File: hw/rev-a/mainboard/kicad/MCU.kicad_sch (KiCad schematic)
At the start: 34 parts, among them J23 MENU_HDR, SW4 RUN, SW5 MENU_BTN, U21 RP2040, Y1 12 MHz

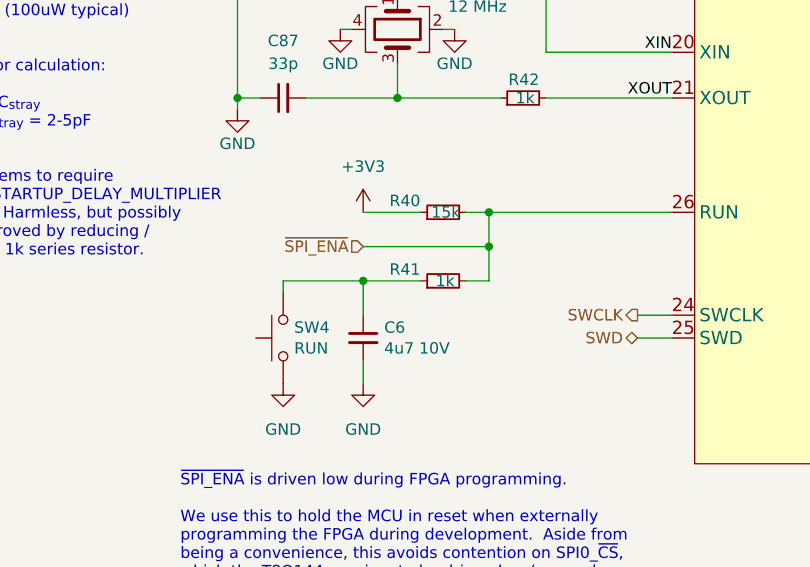
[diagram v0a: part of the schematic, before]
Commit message: hw: use stronger pullup on RUN / SPI_EN, remove debouncing cap
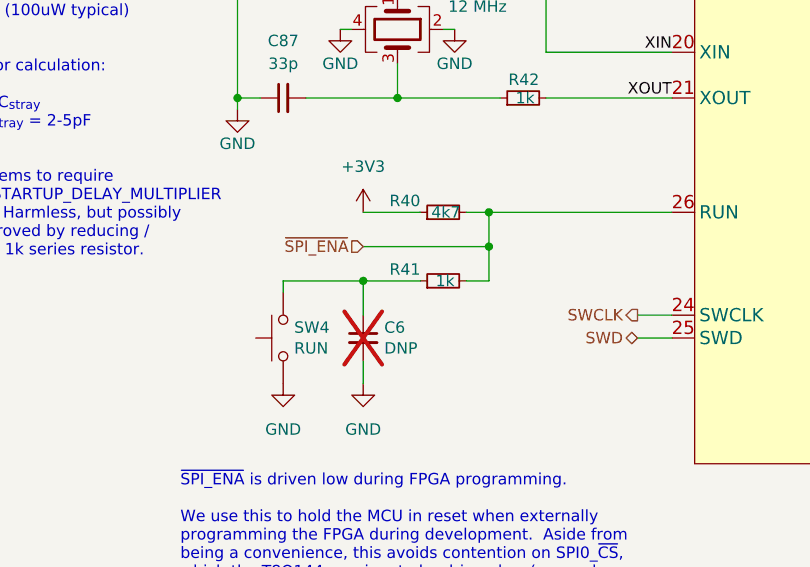
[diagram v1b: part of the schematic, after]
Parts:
- C6: value 4u7 10V -> DNP; LCSC C23733 -> (none); now not fitted
- R40: value 15k -> 4k7; LCSC C25756 -> C25900
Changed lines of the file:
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@@
 		(in_bom yes)
 		(on_board yes)
-		(dnp no)
+		(dnp yes)
 		(property "Reference" "C6"
 			(at 69.6468 120.7516 0)
@@
 			)
 		)
-		(property "Value" "4u7 10V"
+		(property "Value" "DNP"
 			(at 69.6468 123.063 0)
 			(effects
@@
 			)
 		)
-		(property "Datasheet" "https://product.samsungsem.com/mlcc/CL05A475MP5NRN.do"
+		(property "Datasheet" ""
 			(at 67.31 121.92 0)
 			(effects
@@
 			)
 		)
-		(property "LCSC" "C23733"
+		(property "LCSC" ""
 			(at 67.31 121.92 0)
 			(effects
@@
 			)
 		)
-		(property "Value" "15k"
+		(property "Value" "4k7"
 			(at 78.105 107.95 90)
 			(effects
@@
 			)
 		)
-		(property "Datasheet" "https://www.lcsc.com/datasheet/lcsc_datasheet_2206010100_UNI-ROYAL-Uniroyal-Elec-0402WGF1502TCE_C25756.pdf"
+		(property "Datasheet" "https://www.lcsc.com/datasheet/lcsc_datasheet_2206010045_UNI-ROYAL-Uniroyal-Elec-0402WGF4701TCE_C25900.pdf"
 			(at 76.2 107.95 0)
 			(effects
@@
 			)
 		)
-		(property "LCSC" "C25756"
+		(property "LCSC" "C25900"
 			(at 76.2 107.95 0)
 			(effects

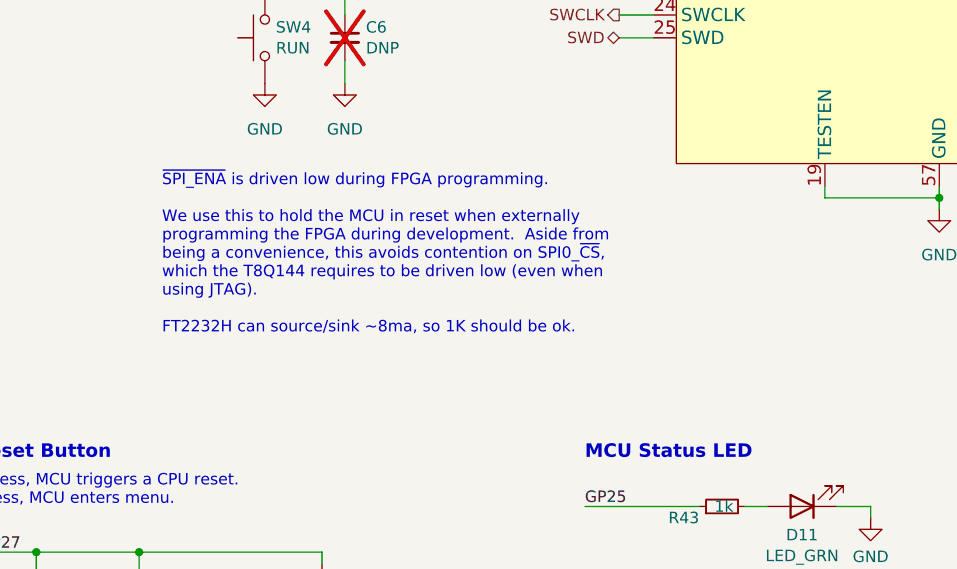
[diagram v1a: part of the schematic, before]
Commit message: hw: document JTAG / RP2040 interaction
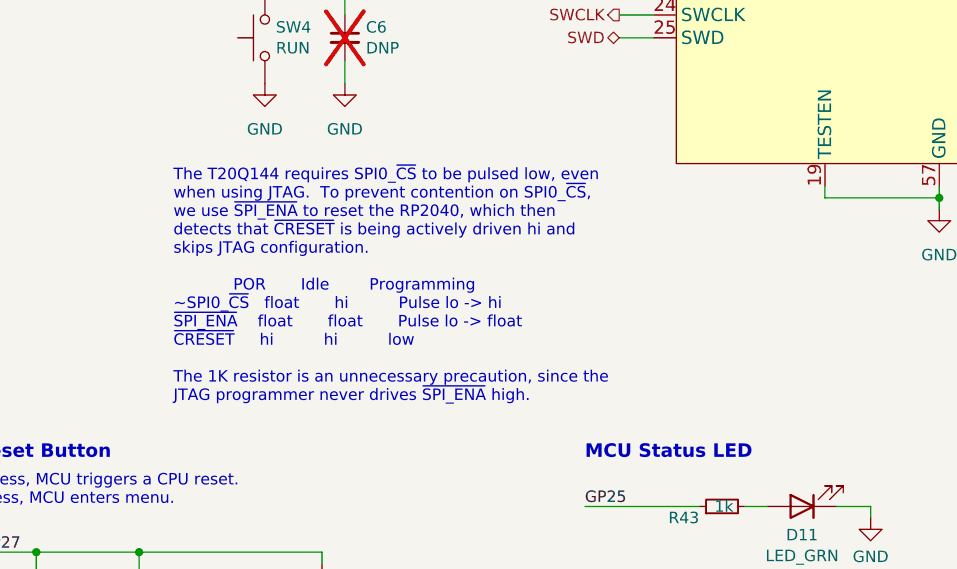
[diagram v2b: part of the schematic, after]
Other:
- note added: "The T20Q144 requires SPI0_~{CS} to be pulsed low, even when using JTAG. To prevent contention on SPI0_~{CS}, we use ~{SPI_ENA} to reset the RP2040, which then detects that ~{CRESET} is being actively driven hi and skips JTAG configuration. POR Idle Programming ~SPI0_~{CS} float hi Pulse lo -> hi ~{SPI_ENA} float float Pulse lo -> float ~{CRESET} hi hi low The 1K resistor is an unnecessary precaut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"
- note removed: "~{SPI_ENA} is driven low during FPGA programming. We use this to hold the MCU in reset when externally programming the FPGA during development. Aside from being a convenience, this avoids contention on SPI0_~{CS}, which the T8Q144 requires to be driven low (even when using JTAG). FT2232H can source/sink ~8ma, so 1K should be ok."
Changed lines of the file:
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@@
 		)
 	)
-	(text "~{SPI_ENA} is driven low during FPGA programming.\n\nWe use this to hold the MCU in reset when externally\nprogramming the FPGA during development.  Aside from\nbeing a convenience, this avoids contention on SPI0_~{CS},\nwhich the T8Q144 requires to be driven low (even when\nusing JTAG).\n\nFT2232H can source/sink ~8ma, so 1K should be ok.\n"
+	(text "The T20Q144 requires SPI0_~{CS} to be pulsed low, even\nwhen using JTAG.  To prevent contention on SPI0_~{CS},\nwe use ~{SPI_ENA} to reset the RP2040, which then\ndetects that ~{CRESET} is being actively driven hi and\nskips JTAG configuration.\n\n            POR       Idle        Programming\n~SPI0_~{CS}   float       hi          Pulse lo -> hi\n~{SPI_ENA}    float       float       Pulse lo -> float\n~{CRESET}     hi          hi          low\n\nThe 1K resistor is an unnecessary precaution, since the\nJTAG programmer never drives ~{SPI_ENA} high.\n"
 		(exclude_from_sim no)
-		(at 46.99 154.94 0)
+		(at 48.26 162.56 0)
 		(effects
 			(font
